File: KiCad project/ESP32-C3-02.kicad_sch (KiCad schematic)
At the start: 30 parts, among them J3 GSD090012SEU, U3 ESP32-C3-WROOM-02-H4, U4 CP2102N-A02-GQFN20, U5 USBLC6-2SC6, U6 W25Q32JVSSIQ

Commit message: Add HX711 scale controller schematic and clean up legacy components
- Add HX711_LoadCell_Summing child sheet with 4x MTMM-103-03-T-S-150 load cell connectors, summing resistors, and decoupling caps
- Add OLED_Header child sheet (4-pin I2C socket for SSD1306)
- Remove battery charger (MCP73871), LiPo connector, mic preamp, BME280, SD card from schematic
- Reconnect power path: +5V_USB -> FB1 -> +5V -> LDO
- Add Samtec MTMM-103-03-T-S-150 footprint library to fp-lib-table
- Assign footprints to HX711 passives (C12-C17, R15/R16) and net ties (NT1-NT3)
- Update PCB from schematic: add new scale components, remove legacy footprints
- Track fp-lib-table in git (uses portable ${KIPRJMOD} paths)

Co-Authored-By: Claude Sonnet 4.6 <noreply@anthropic.com>
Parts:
- removed C12: 10u, Footprints:T491A, symbol T491A106K010AT7280:T491A106K010AT7280
- removed C13, C14: 0.1u, Capacitor_SMD:C_0805_2012Metric, symbol SparkFun-Capacitor:C
- removed J3: GSD090012SEU, Footprints:AMPHENOL_GSD090012SEU, symbol GSD090012SEU:GSD090012SEU
- removed R15, R16, R20, R22: 50, Resistor_SMD:R_0805_2012Metric, symbol Device:R
- removed R19: 10K, Resistor_SMD:R_0805_2012Metric, symbol Device:R
- removed TP1: Test MOSI, TestPoint:TestPoint_Pad_D1.0mm, symbol Connector:TestPoint
- removed TP3: Test CLK, TestPoint:TestPoint_Pad_D1.0mm, symbol Connector:TestPoint
- removed TP5: TEST CS, TestPoint:TestPoint_Pad_D1.0mm, symbol Connector:TestPoint
- removed U6: W25Q32JVSSIQ, Footprints:SOIC127P790X216-8N, symbol W25Q32JVSSIQ:W25Q32JVSSIQ
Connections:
- net DOUT: now reaches U3.5 (IO6)
- net DOUT: now also TP2.1
- net CS: no longer names the net of U3.10 (IO10)
- net CS_SD renamed PD_SCK
- net MIC_OUT: no longer names the net of U3.18 (IO0)
- net MISO_DO: no longer names the net of U3.16 (IO2)
- net MISO_DO: no longer TP2.1
- net PHOTO_C: no longer names the net of U3.17 (IO1)
- no-connect marks 7 -> 10
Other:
- removed sheet Sensors
- sheet User interface ports: added none; removed SCL, SDA
- note removed: "Flash memory"
- note removed: "SD card module"
- company: Tech Explorations -> (none)
- title: ESP32 C3 02 and USB to UART converter -> ESP32 sensor board

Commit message: Fix HX711 input filter topology; remove stale test points
C12/C13 were in series with the load-cell signal (S -> 100R -> 4.7nF ->
INA), which blocks the DC bridge output. R15/R16 now feed INA+/INA-
directly and C12/C13 shunt those nodes to AGND. Removed TP2 (DOUT) and
TP4 (PD_SCK), leftovers from the KLP-5e board. Netlist: 64 nets, ERC 0
errors. PCB updated from schematic; 66 unrouted, DRC unchanged.

Co-Authored-By: Claude Fable 5.1 <noreply@anthropic.com>
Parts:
- removed TP2: Test MISO, TestPoint:TestPoint_Pad_D1.0mm, symbol Connector:TestPoint
- removed TP4: TEST CS_SD, TestPoint:TestPoint_Pad_D1.0mm, symbol Connector:TestPoint
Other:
- note removed: "Test points"
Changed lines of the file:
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@@
-	)
-	(rectangle
-		(start 145.415 24.765)
-		(end 167.005 67.31)
-		(stroke
-			(width 0)
-			(type default)
-		)
-		(fill
-			(type none)
-		)
 	)
 	(rectangle
@@
 		(exclude_from_sim no)
 		(at 24.892 14.224 0)
-		(effects
-			(font
-				(size 1.27 1.27)
-			)
-		)
-	)
-	(text "Test points"
-		(exclude_from_sim no)
-		(at 152.146 23.114 0)
 		(effects
 			(font
@@
 		)
 	)
-	(label "PD_SCK"
-		(at 156.21 54.61 0)
-		(effects
-			(font
-				(size 1.27 1.27)
-			)
-			(justify left bottom)
-		)
-	)
 	(label "RX_TX"
 		(at 92.71 69.85 0)
@@
 	(label "USB_D+"
 		(at 55.88 85.09 0)
-		(effects
-			(font
-				(size 1.27 1.27)
-			)
-			(justify left bottom)
-		)
-	)
-	(label "DOUT"
-		(at 156.21 39.37 0)
 		(effects
 			(font
@@
 	)
 	(symbol
-		(lib_id "Connector:TestPoint")
-		(at 156.21 54.61 90)
-		(unit 1)
-		(exclude_from_sim no)
-		(in_bom yes)
-		(on_board yes)
-		(dnp no)
-		(property "Reference" "TP4"
-			(at 152.908 49.53 90)
-			(effects
-				(font
-					(size 1.27 1.27)
-				)
-			)
-		)
-		(property "Value" "TEST CS_SD"
-			(at 152.908 52.07 90)
-			(effects
-				(font
-					(size 1.27 1.27)
-				)
-			)
-		)
-		(property "Footprint" "TestPoint:TestPoint_Pad_D1.0mm"
-			(at 156.21 49.53 0)
-			(effects
-				(font
-					(size 1.27 1.27)
-				)
-				(hide yes)
-			)
-		)
-		(property "Datasheet" "~"
-			(at 156.21 49.53 0)
-			(effects
-				(font
-					(size 1.27 1.27)
-				)
-				(hide yes)
-			)
-		)
-		(property "Description" "test point"
-			(at 156.21 54.61 0)
-			(effects
-				(font
-					(size 1.27 1.27)
-				)
-				(hide yes)
-			)
-		)
-		(pin "1"
-		)
-		(instances
-			(project "ScaleController_RevA"
-				(path "/16c571a0-8550-4f05-972c-22b0701cbf02/09ec4a32-ddff-43cd-8e21-9ef822101853"
-					(reference "TP4")
-					(unit 1)
-				)
-			)
-		)
-	)
-	(symbol
 		(lib_id "power:GND")
 		(at 53.34 52.07 0)
@@
 					(unit 1)
 				)
-			)
-		)
-	)
-	(symbol
-		(lib_id "Connector:TestPoint")
-		(at 156.21 39.37 90)
-		(unit 1)
-		(exclude_from_sim no)
-		(in_bom yes)
-		(on_board yes)
-		(dnp no)
-		(property "Reference" "TP2"
-			(at 152.908 34.29 90)
-			(effects
-				(font
-					(size 1.27 1.27)
-				)
-			)
-		)
-		(property "Value" "Test MISO"
-			(at 152.908 36.83 90)
-			(effects
-				(font
-					(size 1.27 1.27)
-				)
-			)
-		)
-		(property "Footprint" "TestPoint:TestPoint_Pad_D1.0mm"
-			(at 156.21 34.29 0)
-			(effects
-				(font
-					(size 1.27 1.27)
-				)
-				(hide yes)
-			)
-		)
-		(property "Datasheet" "~"
-			(at 156.21 34.29 0)
-			(effects
-				(font
-					(size 1.27 1.27)
-				)
-				(hide yes)
-			)
-		)
-		(property "Description" "test point"
-			(at 156.21 39.37 0)
-			(effects
-				(font
-					(size 1.27 1.27)
-				)
-				(hide yes)
-			)
-		)
-		(pin "1"
-		)
-		(instances
-			(project "ScaleController_RevA"
-				(path "/16c571a0-8550-4f05-972c-22b0701cbf02/09ec4a32-ddff-43cd-8e21-9ef822101853"
-					(reference "TP2")
-					(unit 1)
-				)

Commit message: Pre-order tidy: DRU, symbol-lib sync, PCBWay stackup, JST part number on J3/5/7/8
- .kicad_dru: drop the global annular_width ignore. U3's ground-grid pads
  are 0.6/0.3 mm since the DFM pass; DRC is identical without the rule.
- Project symbol libs for LM1117MPX-3.3_NOPB, ESP32-C3-WROOM-02-H4 and
  MTMM-103-03-T-S-150 rewritten in KiCad 9 format from the schematic
  copies (the MTMM copy has pins 1/2/3 to match the JST PH pads; the old
  lib still had 01/02/03). SnapEDA "Description_1" junk fields removed
  from libs, embedded copies and instances. ERC: 0 lib_symbol_mismatch.
- Stackup: PCBWay standard 4-layer 1.6 mm (7628 prepreg 0.19 x2,
  core 1.03, 1 oz all layers).
- J3/J5/J7/J8: Value/MF/MP -> JST B3B-PH-K-S in schematic, project lib
  and board footprints; stale Samtec/SnapEDA fields dropped. Symbol name
  and lib_id left as MTMM-103-03-T-S-150.

Netlist nets/pins identical before and after. DRC with schematic parity:
0 errors, 0 unconnected, 0 parity issues, 5 known benign warnings.

Co-Authored-By: Claude Fable 5.1 <noreply@anthropic.com>
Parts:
- U3: Description_1 WiFi Modules (802.11) (Engineering Samples) SMD module, ESP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 -> (none)
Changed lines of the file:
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@@
-			)
-		)
-		(property "Description_1" "\n                        \n                            WiFi Modules (802.11) (Engineering Samples) SMD module, ESP32-C3, 4MB SPI flash, PCB antenna, -40 C +105 C\n                        \n"
-			(at 215.9 44.45 0)
-			(effects
-				(font
-					(size 1.27 1.27)
-				)
-				(justify bottom)
-				(hide yes)
 			)
 		)

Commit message: BOM fixes, DRC exclusions, edge-clearance restore, fab outputs and order notes
- C9 value 4.7u -> 10u (matches its KEMET T491A 10 uF part number; LM1117
  output cap). Capacitor values normalised to 0.1u / 1u / 10u so identical
  0805 parts group: BOM 30 -> 27 lines.
- J1 value -> HRO TYPE-C-31-M-12, MF/MP fields added (schematic + board).
- min_copper_edge_clearance restored to 0.3 mm. The DFM commit 4617449 set
  it; the GUI refill save in 61ca090 wrote the old project file back (0.2).
  Board meets 0.3 (probe rule: no violations).
- DRC exclusions for the 4 silk-over-edge warnings (J1 face, U3 antenna
  notch), added in the GUI.
- docs/pcbway-order-notes.md: board spec, stackup, drills, special notes.
- docs/status-2026-09-18.md: supersedes 17 Sept; kicad-cli regen commands.
- TODO: fabrication items ticked.

Fab package generated to fabrication/RevA-2026-09-18/ (git-ignored):
schematic PDF, BOM (raw + PCBWay), Gerbers/drill zip, pos top/bottom.
Netlist nets/pins identical to bdae270. DRC + parity: 0 errors,
0 unconnected, 0 parity; 4 excluded + 1 intentional warning.

Co-Authored-By: Claude Fable 5.1 <noreply@anthropic.com>
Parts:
- C9: value 4.7u -> 10u
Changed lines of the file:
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@@
 			)
 		)
-		(property "Value" "4.7u"
+		(property "Value" "10u"
 			(at 70.358 33.528 0)
 			(effects

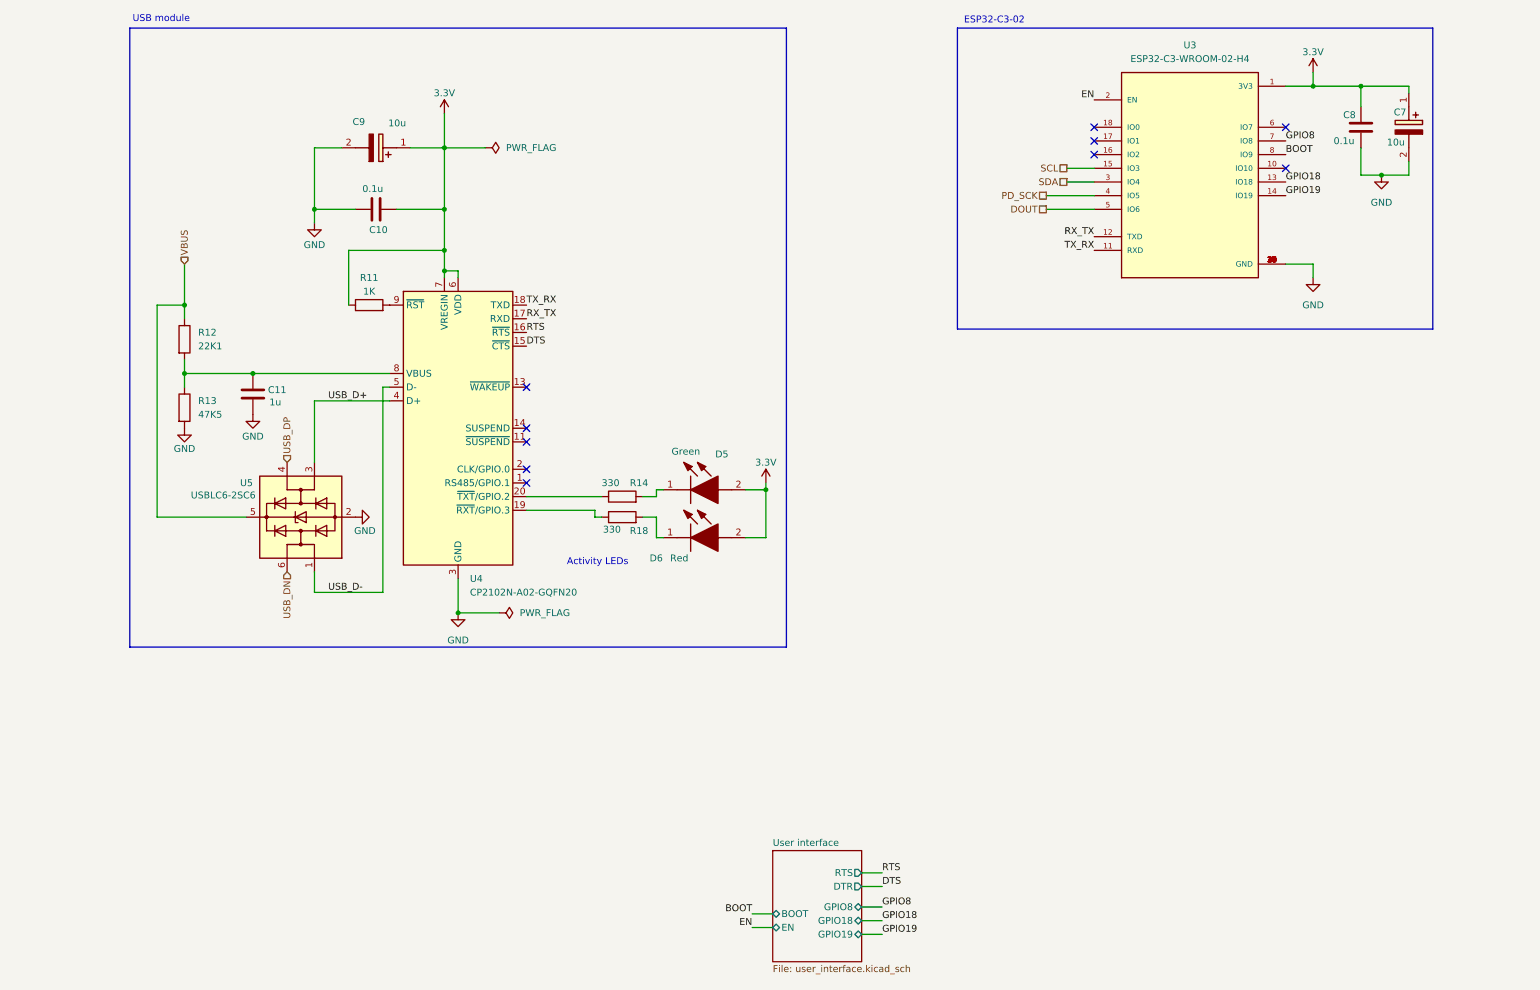
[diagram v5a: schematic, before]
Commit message: Schematic: native USB-Serial/JTAG replaces the CP2102N; strapping and I2C pull-ups; status LED
Review findings F1-F5 (docs/schematic-review-2026-09-18.md), Level 1 + 2:
- Removed U4 CP2102N and its support parts (R11, R12, R13, C9, C10, C11,
  D6, R18) and the DTR/RTS auto-program circuit (Q2, Q3, R33, R34).
  The QFN20 CP2102N has no DTR, so that circuit could never work.
- USB D+/D- now run from the ESD diode U5 to the module's native USB pins
  (IO19 = USB_D+, IO18 = USB_D-). Reset and download-mode entry are handled
  by the USB-Serial/JTAG peripheral.
- Pull-ups: R3 10k GPIO8 (required high for download boot), R4 10k GPIO2
  (recommended), R5 10k GPIO9/BOOT, R6/R7 4.7k SDA/SCL.
- D5 (green) + R14 kept as a status LED on GPIO7 (active-low).
- J6 expansion header re-pinned: 3.3V, GPIO10, U0TXD, U0RXD, GND.
- PWR_FLAG on GND moved to U5 (the one on the CP2102N ground went with it).
- firmware: logger on USB_SERIAL_JTAG, status_led on GPIO7, pin map notes.

ERC: 0 errors. Netlist connectivity checked pin-by-pin against the
intended design. Board not yet updated: run Update PCB from Schematic.

Co-Authored-By: Claude Fable 5.1 <noreply@anthropic.com>
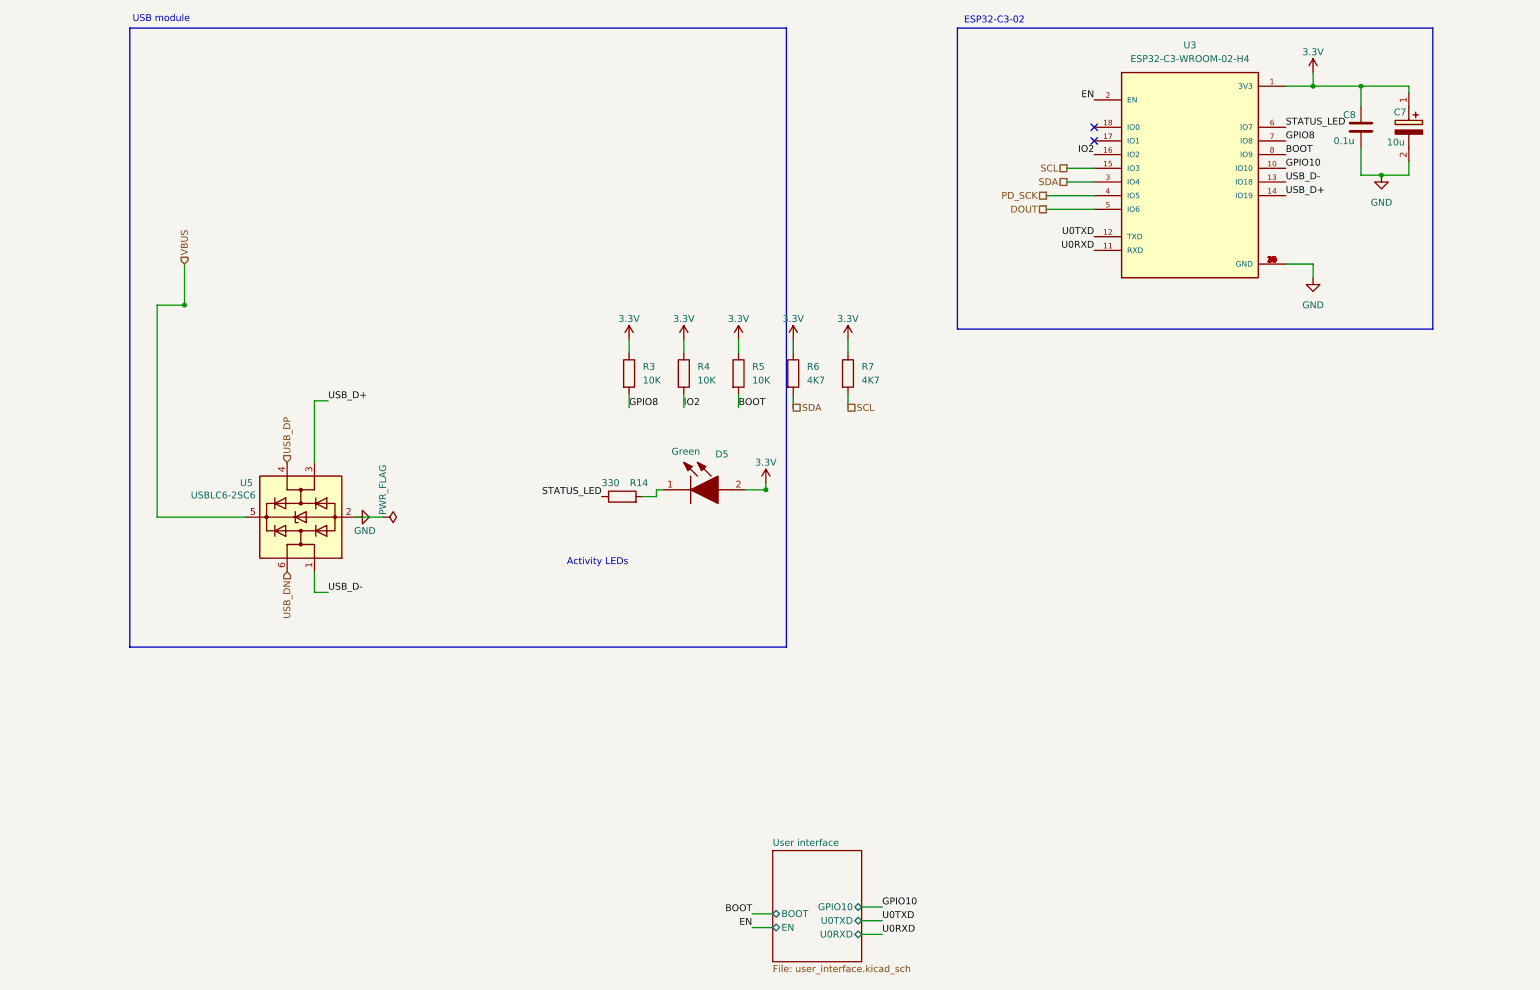
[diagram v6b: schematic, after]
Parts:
- removed C10: 0.1u, Capacitor_SMD:C_0805_2012Metric, symbol SparkFun-Capacitor:C
- removed C11: 1u, Capacitor_SMD:C_0805_2012Metric, symbol SparkFun-Capacitor:C
- removed C9: 10u, Footprints:T491A, symbol T491A106K010AT7280:T491A106K010AT7280
- removed D6: Red, Footprints:LEDC2012X120N, symbol LTST-C170KRKT:LTST-C170KRKT
- removed R11: 1K, Resistor_SMD:R_0805_2012Metric, symbol Device:R
- removed R12: 22K1, Resistor_SMD:R_0805_2012Metric, symbol Device:R
- removed R13: 47K5, Resistor_SMD:R_0805_2012Metric, symbol Device:R
- removed R18: 330, Resistor_SMD:R_0805_2012Metric, symbol Device:R
- removed U4: CP2102N-A02-GQFN20, Package_DFN_QFN:SiliconLabs_QFN-20-1EP_3x3mm_P0.5mm_EP1.8x1.8mm, symbol Interface_USB:CP2102N-Axx-xQFN20
- added R3, R4, R5: 10K, Resistor_SMD:R_0805_2012Metric, symbol Device:R
- added R6, R7: 4K7, Resistor_SMD:R_0805_2012Metric, symbol Device:R
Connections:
- net GPIO18 is gone; now on net USB_D-: U3.13 (IO18)
- net GPIO19 is gone; now on net USB_D+: U3.14 (IO19)
- net 3.3V: now also R3.1, R4.1, R5.1, R6.1, R7.1
- net BOOT: now also R5.2
- net GPIO8: now also R3.2
- net SCL: now also R7.2
- net SDA: now also R6.2
- net STATUS_LED: now reaches R14.1
- net STATUS_LED: now also U3.6 (IO7)
- net GPIO10: now reaches U3.10 (IO10)
- net IO2: now reaches U3.16 (IO2)
- net IO2: now also R4.2
- net RX_TX renamed U0TXD
- net TX_RX renamed U0RXD
- no-connect marks 10 -> 2
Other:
- sheet User interface ports: added GPIO10, U0RXD, U0TXD; removed DTR, GPIO18, GPIO19, GPIO8, RTS

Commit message: Schematic: refresh sheet captions after the USB rework; drop the stale auto-program table
Co-Authored-By: Claude Fable 5.1 <noreply@anthropic.com>
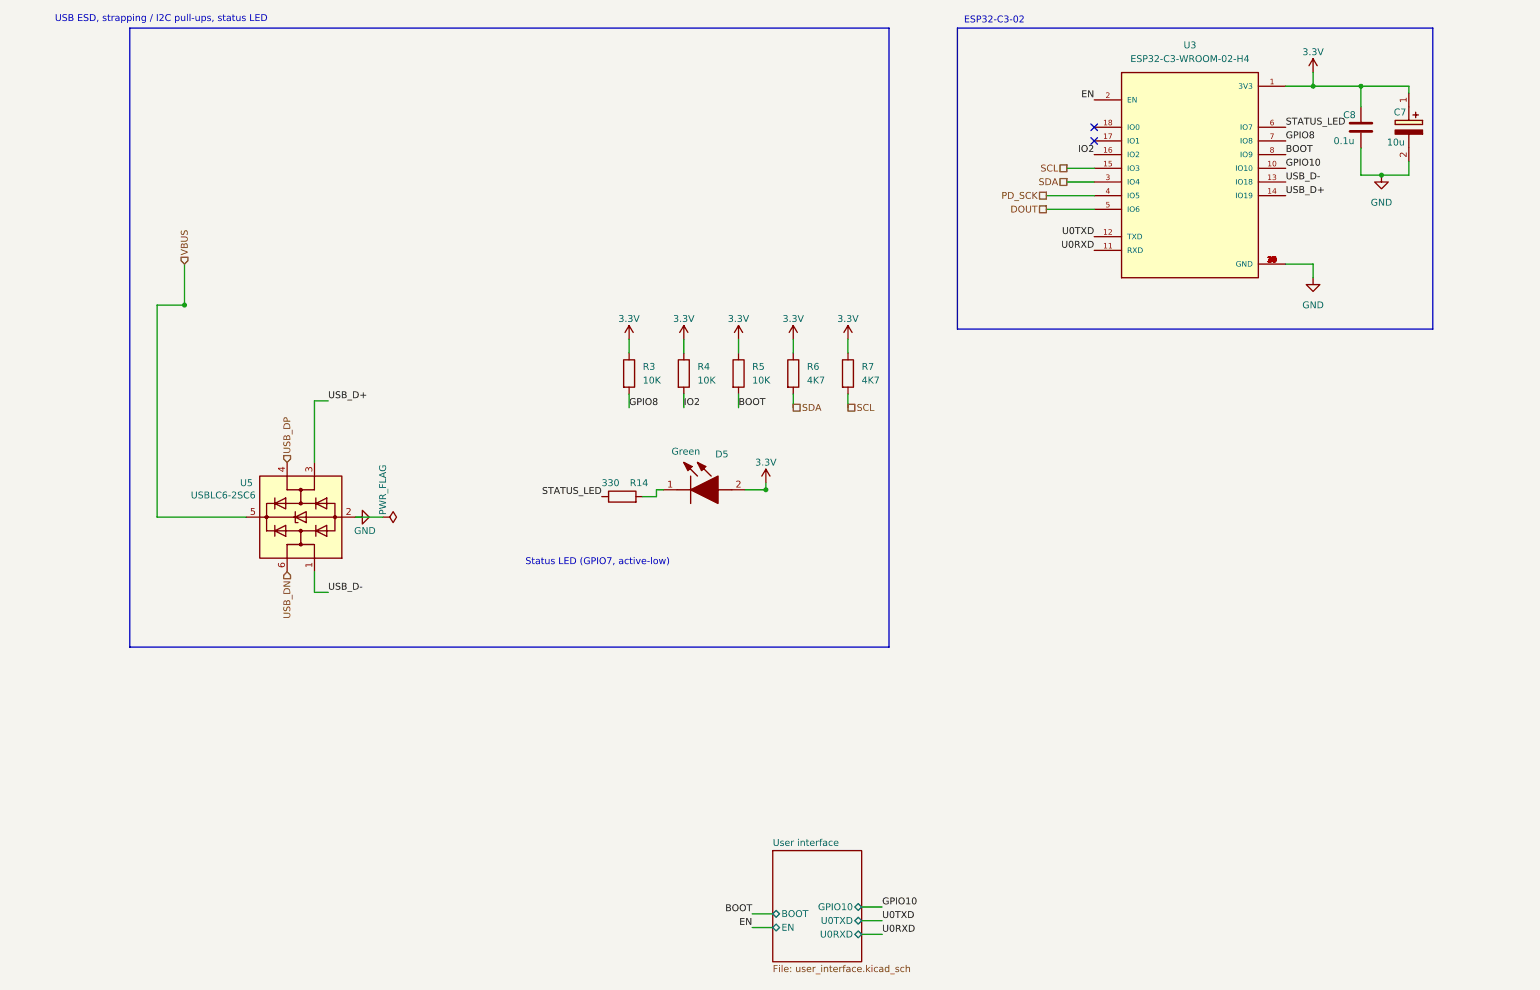
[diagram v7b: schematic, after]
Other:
- note added: "Status LED (GPIO7, active-low)"
- note added: "USB ESD, strapping / I2C pull-ups, status LED"
- note removed: "Activity LEDs"
- note removed: "USB module"
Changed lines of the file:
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@@
 	(rectangle
 		(start 19.05 15.875)
-		(end 140.97 130.81)
+		(end 160.02 130.81)
 		(stroke
 			(width 0)
@@
 		)
 	)
-	(text "Activity LEDs"
+	(text "Status LED (GPIO7, active-low)"
 		(exclude_from_sim no)
 		(at 105.918 115.062 0)
@@
 		)
 	)
-	(text "USB module"
+	(text "USB ESD, strapping / I2C pull-ups, status LED"
 		(exclude_from_sim no)
 		(at 24.892 14.224 0)

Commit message: Schematic: title blocks (Scale Controller, rev A, 2026-09-18, per-sheet comments); replace stale CP2102 and ESP32-S3 notes
Co-Authored-By: Claude Fable 5.1 <noreply@anthropic.com>
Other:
- company: (none) -> Steve Maegley
- title: ESP32 sensor board -> Scale Controller
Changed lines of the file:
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@@
 	(paper "A4")
 	(title_block
-		(title "ESP32 sensor board")
-		(date "2024-11-23")
-		(rev "1")
-		(comment 1 "OLED Header")
+		(title "Scale Controller")
+		(date "2026-09-18")
+		(rev "A")
+		(company "Steve Maegley")
+		(comment 1 "ESP32-C3 module, native USB, pull-ups, status LED")
 	)
 	(rectangle
